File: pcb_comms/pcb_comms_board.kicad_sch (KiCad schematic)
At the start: 0 parts

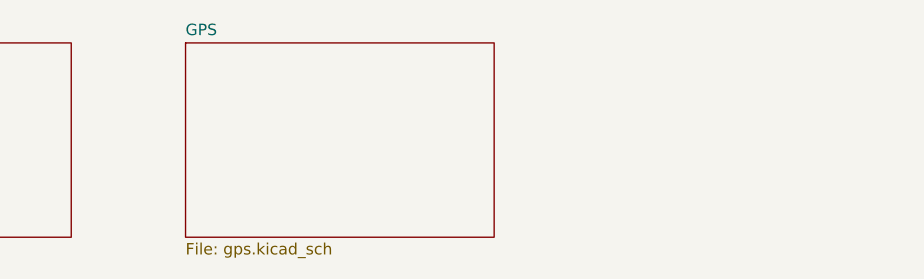
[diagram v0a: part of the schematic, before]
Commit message: Add usb and gps
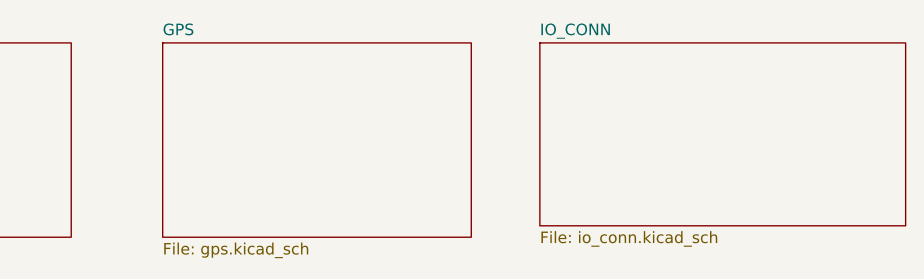
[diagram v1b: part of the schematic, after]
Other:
- added sheet IO_CONN (io_conn.kicad_sch)
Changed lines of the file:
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@@
 	(paper "A4")
 	(sheet
-		(at 135.89 31.75)
+		(at 133.35 31.75)
 		(size 34.29 21.59)
 		(exclude_from_sim no)
@@
 		)
 		(property "Sheetname" "GPS"
-			(at 135.89 31.0384 0)
+			(at 133.35 31.0384 0)
 			(effects
 				(font
@@
 		)
 		(property "Sheetfile" "gps.kicad_sch"
-			(at 135.89 53.9246 0)
+			(at 133.35 53.9246 0)
 			(effects
 				(font
@@
 				)
 			)
+		)
+	)
+	(sheet
+		(at 175.26 31.75)
+		(size 40.64 20.32)
+		(exclude_from_sim no)
+		(in_bom yes)
+		(on_board yes)
+		(dnp no)
+		(fields_autoplaced yes)
+		(stroke
+			(width 0.1524)
+			(type solid)
+		)
+		(fill
+			(color 0 0 0 0.0000)
+		)
+		(property "Sheetname" "IO_CONN"
+			(at 175.26 31.0384 0)
+			(effects
+				(font
+					(size 1.27 1.27)
+				)
+				(justify left bottom)
+			)
+		)
+		(property "Sheetfile" "io_conn.kicad_sch"
+			(at 175.26 52.6546 0)
+			(effects
+				(font
+					(size 1.27 1.27)
+				)
+				(justify left top)
+			)
+		)
+		(instances
+			(project "pcb_comms_board"
+				(path "/ea597178-b44d-4db9-826c-8f86e8d231f0"
+					(page "5")
+				)
+			)

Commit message: Update GPS
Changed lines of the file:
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@@
 	(sheet
 		(at 175.26 31.75)
-		(size 40.64 20.32)
+		(size 35.56 20.32)
 		(exclude_from_sim no)
 		(in_bom yes)

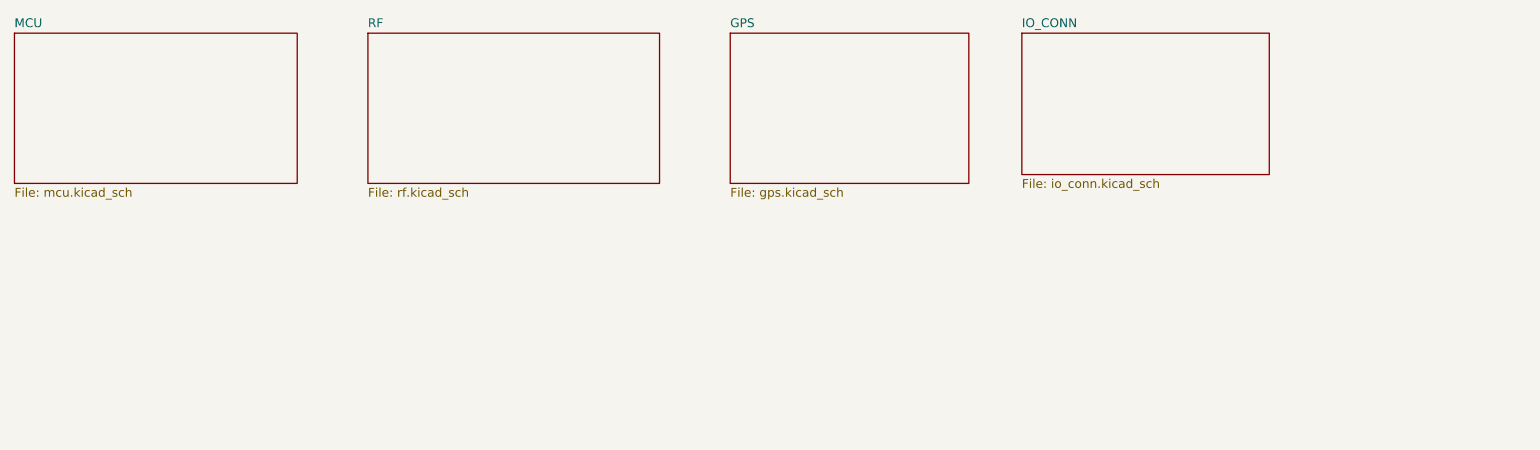
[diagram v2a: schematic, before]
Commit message: Add antenna deploy
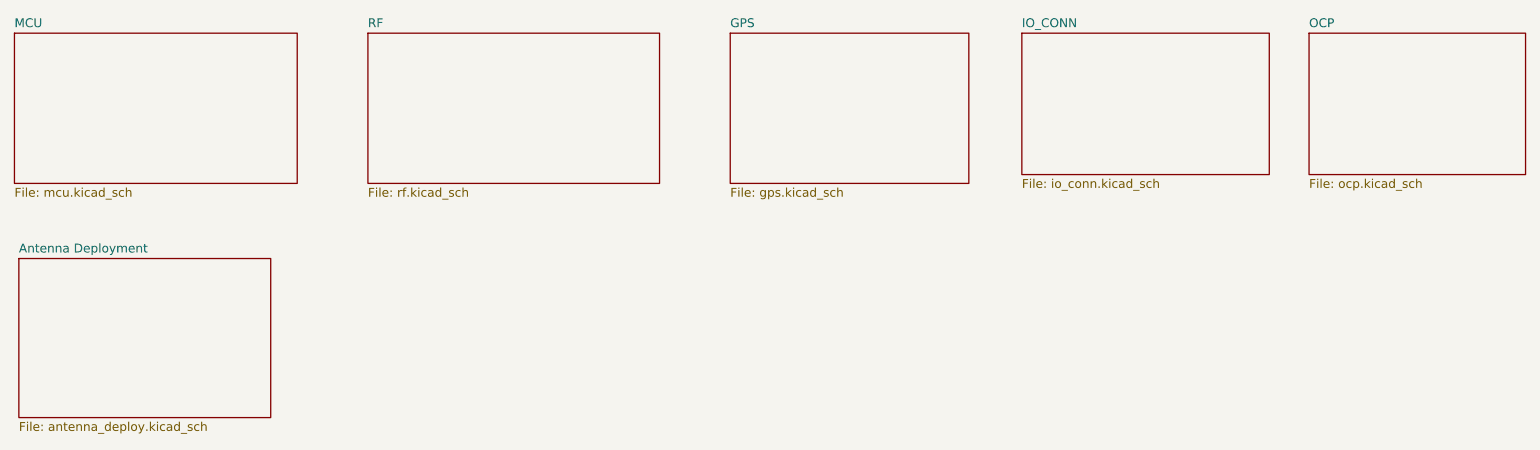
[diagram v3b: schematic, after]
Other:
- added sheet Antenna Deployment (antenna_deploy.kicad_sch)
- added sheet OCP (ocp.kicad_sch)
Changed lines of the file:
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@@
 	(paper "A4")
+	(sheet
+		(at 216.535 31.75)
+		(size 31.115 20.32)
+		(exclude_from_sim no)
+		(in_bom yes)
+		(on_board yes)
+		(dnp no)
+		(fields_autoplaced yes)
+		(stroke
+			(width 0.1524)
+			(type solid)
+		)
+		(fill
+			(color 0 0 0 0.0000)
+		)
+		(property "Sheetname" "OCP"
+			(at 216.535 31.0384 0)
+			(effects
+				(font
+					(size 1.27 1.27)
+				)
+				(justify left bottom)
+			)
+		)
+		(property "Sheetfile" "ocp.kicad_sch"
+			(at 216.535 52.6546 0)
+			(effects
+				(font
+					(size 1.27 1.27)
+				)
+				(justify left top)
+			)
+		)
+		(instances
+			(project "pcb_comms_board"
+				(path "/ea597178-b44d-4db9-826c-8f86e8d231f0"
+					(page "6")
+				)
+			)
+		)
+	)
+	(sheet
+		(at 31.115 64.135)
+		(size 36.195 22.86)
+		(exclude_from_sim no)
+		(in_bom yes)
+		(on_board yes)
+		(dnp no)
+		(fields_autoplaced yes)
+		(stroke
+			(width 0.1524)
+			(type solid)
+		)
+		(fill
+			(color 0 0 0 0.0000)
+		)
+		(property "Sheetname" "Antenna Deployment"
+			(at 31.115 63.4234 0)
+			(effects
+				(font
+					(size 1.27 1.27)
+				)
+				(justify left bottom)
+			)
+		)
+		(property "Sheetfile" "antenna_deploy.kicad_sch"
+			(at 31.115 87.5796 0)
+			(effects
+				(font
+					(size 1.27 1.27)
+				)
+				(justify left top)
+			)
+		)
+		(instances
+			(project "pcb_comms_board"
+				(path "/ea597178-b44d-4db9-826c-8f86e8d231f0"
+					(page "7")
+				)
+			)
+		)
+	)
 	(sheet
 		(at 133.35 31.75)

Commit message: Last update
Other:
- company: (none) -> Sanie Peralta, Alejandro Campo
- title: (none) -> PC1: APRS & GPS
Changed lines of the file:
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@@
 	(generator_version "9.0")
 	(paper "A4")
+	(title_block
+		(title "PC1: APRS & GPS")
+		(date "2026-04-01")
+		(rev "1.0")
+		(company "Sanie Peralta, Alejandro Campo")
+		(comment 1 "Introducción a la Ingeniería Satelital ")
+		(comment 2 "Primer Parcial")
+	)
 	(sheet
 		(at 216.535 31.75)

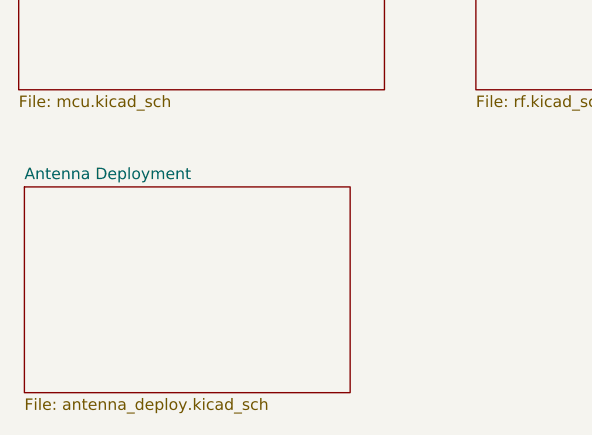
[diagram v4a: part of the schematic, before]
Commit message: Finish schematic
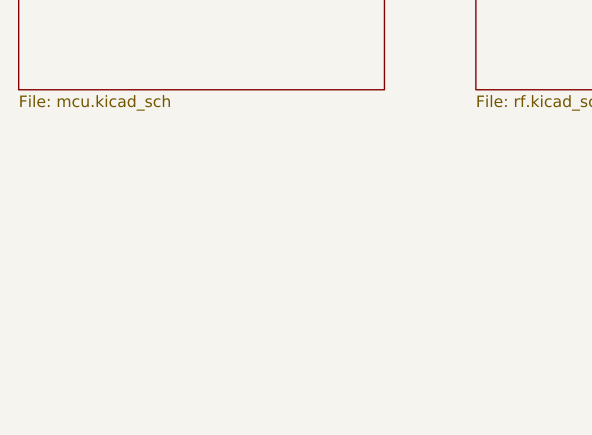
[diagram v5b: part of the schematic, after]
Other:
- removed sheet Antenna Deployment
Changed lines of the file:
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@@
-	)
-	(sheet
-		(at 31.115 64.135)
-		(size 36.195 22.86)
-		(exclude_from_sim no)
-		(in_bom yes)
-		(on_board yes)
-		(dnp no)
-		(fields_autoplaced yes)
-		(stroke
-			(width 0.1524)
-			(type solid)
-		)
-		(fill
-			(color 0 0 0 0.0000)
-		)
-		(property "Sheetname" "Antenna Deployment"
-			(at 31.115 63.4234 0)
-			(effects
-				(font
-					(size 1.27 1.27)
-				)
-				(justify left bottom)
-			)
-		)
-		(property "Sheetfile" "antenna_deploy.kicad_sch"
-			(at 31.115 87.5796 0)
-			(effects
-				(font
-					(size 1.27 1.27)
-				)
-				(justify left top)
-			)
-		)
-		(instances
-			(project "pcb_comms_board"
-				(path "/ea597178-b44d-4db9-826c-8f86e8d231f0"
-					(page "7")
-				)
-			)
-		)
 	)
 	(sheet

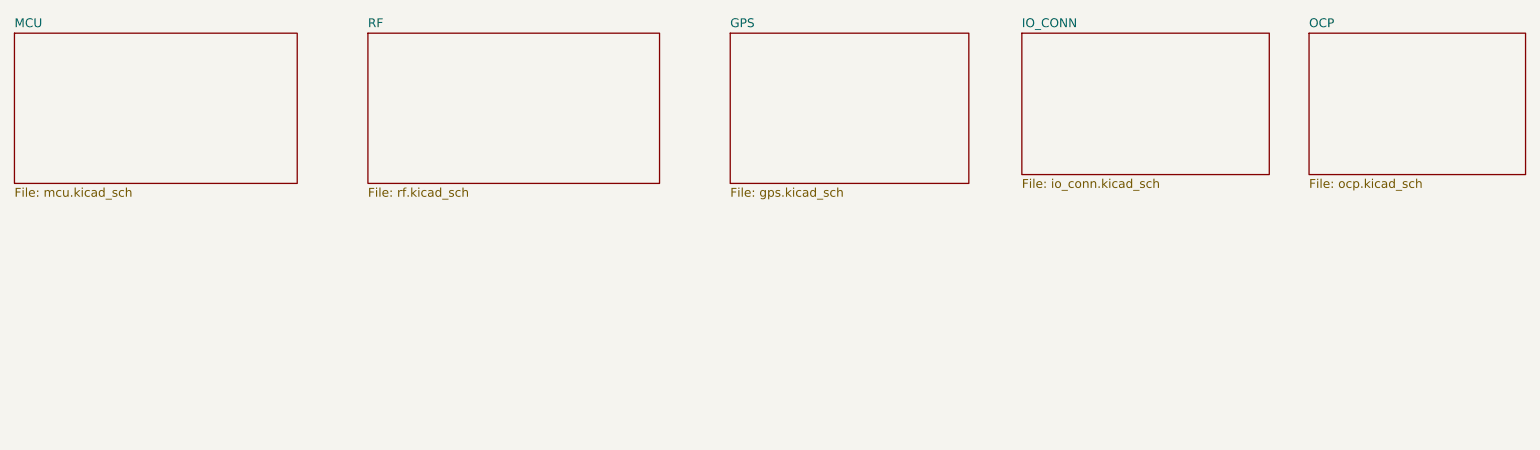
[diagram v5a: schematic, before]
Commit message: remove gps
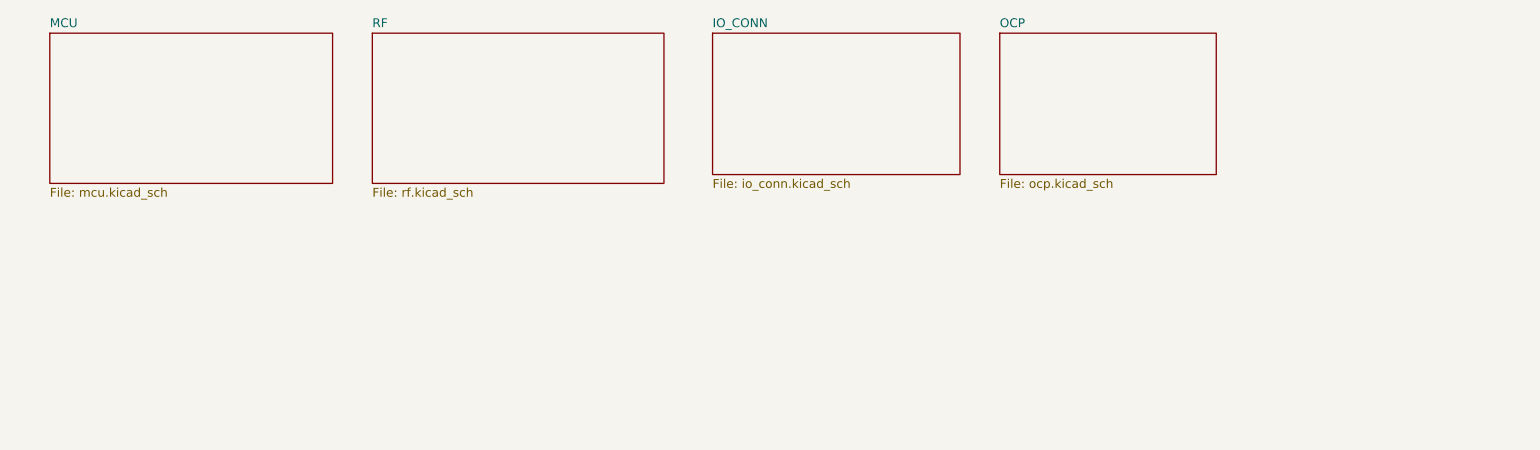
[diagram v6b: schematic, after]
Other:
- removed sheet GPS
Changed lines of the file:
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@@
 	)
 	(sheet
-		(at 216.535 31.75)
+		(at 172.085 31.75)
 		(size 31.115 20.32)
 		(exclude_from_sim no)
@@
 		)
 		(property "Sheetname" "OCP"
-			(at 216.535 31.0384 0)
+			(at 172.085 31.0384 0)
 			(effects
 				(font
@@
 		)
 		(property "Sheetfile" "ocp.kicad_sch"
-			(at 216.535 52.6546 0)
+			(at 172.085 52.6546 0)
 			(effects
 				(font
@@
 	)
 	(sheet
-		(at 133.35 31.75)
-		(size 34.29 21.59)
-		(exclude_from_sim no)
-		(in_bom yes)
-		(on_board yes)
-		(dnp no)
-		(fields_autoplaced yes)
-		(stroke
-			(width 0.1524)
-			(type solid)
-		)
-		(fill
-			(color 0 0 0 0.0000)
-		)
-		(property "Sheetname" "GPS"
-			(at 133.35 31.0384 0)
-			(effects
-				(font
-					(size 1.27 1.27)
-				)
-				(justify left bottom)
-			)
-		)
-		(property "Sheetfile" "gps.kicad_sch"
-			(at 133.35 53.9246 0)
-			(effects
-				(font
-					(size 1.27 1.27)
-				)
-				(justify left top)
-			)
-		)
-		(instances
-			(project "pcb_comms_board"
-				(path "/ea597178-b44d-4db9-826c-8f86e8d231f0"
-					(page "4")
-				)
-			)
-		)
-	)
-	(sheet
-		(at 175.26 31.75)
+		(at 130.81 31.75)
 		(size 35.56 20.32)
 		(exclude_from_sim no)
@@
 		)
 		(property "Sheetname" "IO_CONN"
-			(at 175.26 31.0384 0)
+			(at 130.81 31.0384 0)
 			(effects
 				(font
@@
 		)
 		(property "Sheetfile" "io_conn.kicad_sch"
-			(at 175.26 52.6546 0)
+			(at 130.81 52.6546 0)
 			(effects
 				(font
@@
 	)
 	(sheet
-		(at 30.48 31.75)
+		(at 35.56 31.75)
 		(size 40.64 21.59)
 		(exclude_from_sim no)
@@
 		)
 		(property "Sheetname" "MCU"
-			(at 30.48 31.0384 0)
+			(at 35.56 31.0384 0)
 			(effects
 				(font
@@
 		)
 		(property "Sheetfile" "mcu.kicad_sch"
-			(at 30.48 53.9246 0)
+			(at 35.56 53.9246 0)
 			(effects
 				(font
@@
 	)
 	(sheet
-		(at 81.28 31.75)
+		(at 81.915 31.75)
 		(size 41.91 21.59)
 		(exclude_from_sim no)
@@
 		)
 		(property "Sheetname" "RF"
-			(at 81.28 31.0384 0)
+			(at 81.915 31.0384 0)
 			(effects
 				(font
@@
 		)
 		(property "Sheetfile" "rf.kicad_sch"
-			(at 81.28 53.9246 0)
+			(at 81.915 53.9246 0)
 			(effects
 				(font

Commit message: Update DRA
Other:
- added sheet APRS_RADIO (aprs_radio.kicad_sch)
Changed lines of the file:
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@@
+	)
+	(sheet
+		(at 210.185 31.75)
+		(size 29.21 20.955)
+		(exclude_from_sim no)
+		(in_bom yes)
+		(on_board yes)
+		(dnp no)
+		(fields_autoplaced yes)
+		(stroke
+			(width 0.1524)
+			(type solid)
+		)
+		(fill
+			(color 0 0 0 0.0000)
+		)
+		(property "Sheetname" "APRS_RADIO"
+			(at 210.185 31.0384 0)
+			(effects
+				(font
+					(size 1.27 1.27)
+				)
+				(justify left bottom)
+			)
+		)
+		(property "Sheetfile" "aprs_radio.kicad_sch"
+			(at 210.185 53.2896 0)
+			(effects
+				(font
+					(size 1.27 1.27)
+				)
+				(justify left top)
+			)
+		)
+		(instances
+			(project "pcb_comms_board"
+				(path "/ea597178-b44d-4db9-826c-8f86e8d231f0"
+					(page "6")
+				)
+			)
+		)
 	)
 	(sheet

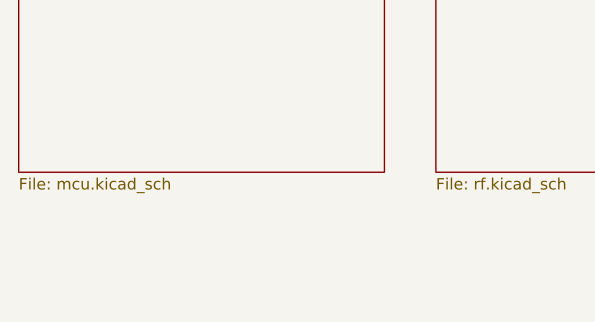
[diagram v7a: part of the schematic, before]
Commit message: Update schematic. Add net classes and JST footprints for aux
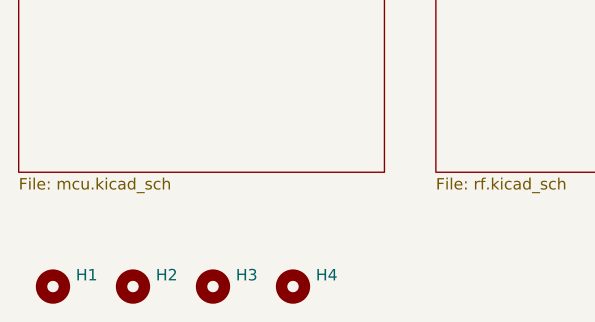
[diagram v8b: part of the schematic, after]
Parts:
- added H1, H2, H3, H4: MountingHole, MountingHole:MountingHole_3.2mm_M3_Pad_Via, symbol Mechanical:MountingHole
